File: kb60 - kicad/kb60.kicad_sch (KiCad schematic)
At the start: 0 parts

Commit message: made schematic for led matrix
also imported scottokeebs library
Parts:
- added D1, D10, D11, D12, D13, D14, D15, D16, D17, D18, D19, D2, D20, D21, D22, D23, D24, D25, D26, D27, D28, D29, D3, D30, D31, D32, D33, D34, D35, D36, D37, D38, D39, D4, D40, D41, D43, D44, D45, D46, D47, D48, D49, D5, D50, D51, D52, D53, D54, D55, D56, D57, D58, D59, D6, D60, D61, D62, D63, D67, D7, D71, D72, D73, D74, D75, D8, D9: Diode, symbol scottokeebs:Placeholder_Diode
- added S1, S10, S11, S12, S13, S14, S15, S16, S17, S18, S19, S2, S20, S21, S22, S23, S24, S25, S26, S27, S28, S29, S3, S30, S31, S32, S33, S34, S35, S36, S37, S38, S39, S4, S40, S41, S43, S44, S45, S46, S47, S48, S49, S5, S50, S51, S52, S53, S54, S55, S56, S57, S58, S59, S6, S60, S61, S62, S63, S67, S7, S71, S72, S73, S74, S75, S8, S9: Keyswitch, symbol scottokeebs:Placeholder_Keyswitch
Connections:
- new net: D16.1 (K), D17.1 (K), D18.1 (K), D19.1 (K), D20.1 (K), D21.1 (K), D22.1 (K), D23.1 (K), D24.1 (K), D25.1 (K), D26.1 (K), D27.1 (K), D28.1 (K), D29.1 (K), D30.1 (K)
- new net: D22.2 (A), S22.2
- new net: D46.1 (K), D47.1 (K), D48.1 (K), D49.1 (K), D50.1 (K), D51.1 (K), D52.1 (K), D53.1 (K), D54.1 (K), D55.1 (K), D56.1 (K), D57.1 (K), D58.1 (K), D59.1 (K), D60.1 (K)
- new net: D59.2 (A), S59.2
- new net: S1.1, S16.1, S31.1, S46.1, S61.1
- new net: D16.2 (A), S16.2
- new net: S15.1, S30.1, S45.1, S60.1, S75.1
- new net: D15.2 (A), S15.2
- new net: D27.2 (A), S27.2
- new net: S11.1, S26.1, S41.1, S56.1, S71.1
- new net: D26.2 (A), S26.2
- new net: D1.1 (K), D10.1 (K), D11.1 (K), D12.1 (K), D13.1 (K), D14.1 (K), D15.1 (K), D2.1 (K), D3.1 (K), D4.1 (K), D5.1 (K), D6.1 (K), D7.1 (K), D8.1 (K), D9.1 (K)
- new net: D10.2 (A), S10.2
- new net: D13.2 (A), S13.2
- new net: D61.1 (K), D62.1 (K), D63.1 (K), D67.1 (K), D71.1 (K), D72.1 (K), D73.1 (K), D74.1 (K), D75.1 (K)
- new net: D74.2 (A), S74.2
- new net: S23.1, S38.1, S53.1, S8.1
- new net: D53.2 (A), S53.2
- new net: D75.2 (A), S75.2
- new net: S21.1, S36.1, S51.1, S6.1
- new net: D21.2 (A), S21.2
- new net: D11.2 (A), S11.2
- new net: D14.2 (A), S14.2
- new net: D71.2 (A), S71.2
- new net: D6.2 (A), S6.2
- new net: D67.2 (A), S67.2
- new net: D1.2 (A), S1.2
- new net: D48.2 (A), S48.2
- new net: S14.1, S29.1, S44.1, S59.1, S74.1
- new net: D29.2 (A), S29.2
- new net: D31.1 (K), D32.1 (K), D33.1 (K), D34.1 (K), D35.1 (K), D36.1 (K), D37.1 (K), D38.1 (K), D39.1 (K), D40.1 (K), D41.1 (K), D43.1 (K), D44.1 (K), D45.1 (K)
- new net: D39.2 (A), S39.2
- new net: D23.2 (A), S23.2
- new net: D44.2 (A), S44.2
- new net: D49.2 (A), S49.2
- new net: D60.2 (A), S60.2
- new net: D40.2 (A), S40.2
- new net: S12.1, S27.1, S57.1, S72.1
- new net: D57.2 (A), S57.2
- new net: S20.1, S35.1, S5.1, S50.1
- new net: D35.2 (A), S35.2
- new net: D50.2 (A), S50.2
- new net: D3.2 (A), S3.2
- new net: D19.2 (A), S19.2
- new net: S10.1, S25.1, S40.1, S55.1
- new net: D72.2 (A), S72.2
- new net: S24.1, S39.1, S54.1, S9.1
- new net: D9.2 (A), S9.2
- new net: S19.1, S34.1, S4.1, S49.1
- new net: D4.2 (A), S4.2
- new net: D17.2 (A), S17.2
- new net: S18.1, S3.1, S33.1, S48.1, S63.1
- new net: D33.2 (A), S33.2
- new net: D54.2 (A), S54.2
- new net: S22.1, S37.1, S52.1, S67.1, S7.1
- new net: D7.2 (A), S7.2
- new net: D63.2 (A), S63.2
- new net: D46.2 (A), S46.2
- new net: S17.1, S2.1, S32.1, S47.1, S62.1
- new net: D47.2 (A), S47.2
- new net: D34.2 (A), S34.2
- new net: D31.2 (A), S31.2
- new net: D38.2 (A), S38.2
- new net: D62.2 (A), S62.2
- new net: D24.2 (A), S24.2
- new net: D18.2 (A), S18.2
- new net: D32.2 (A), S32.2
- new net: D12.2 (A), S12.2
- new net: D20.2 (A), S20.2
- new net: D73.2 (A), S73.2
- new net: D5.2 (A), S5.2
- new net: D2.2 (A), S2.2
- new net: D36.2 (A), S36.2
- new net: D51.2 (A), S51.2
- new net: D41.2 (A), S41.2
- new net: D37.2 (A), S37.2
- new net: D25.2 (A), S25.2
- new net: D28.2 (A), S28.2
- new net: D55.2 (A), S55.2
- new net: S13.1, S28.1, S43.1, S58.1, S73.1
- new net: D52.2 (A), S52.2
- new net: D43.2 (A), S43.2
- new net: D56.2 (A), S56.2
- new net: D30.2 (A), S30.2
- new net: D61.2 (A), S61.2
- new net: D58.2 (A), S58.2
- new net: D45.2 (A), S45.2
- new net: D8.2 (A), S8.2

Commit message: completed schematic
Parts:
- added U1: Raspberry_Pi_Pico, ScottoKeebs_MCU:Raspberry_Pi_Pico, symbol scottokeebs:MCU_Raspberry_Pi_Pico
- D1, D10, D11, D12, D13, D14, D15, D16, D17, D18, D19, D2, D20, D21, D22, D23, D24, D25, D26, D27, D28, D29, D3, D30, D31, D32, D33, D34, D35, D36, D37, D38, D39, D4, D40, D41, D43, D44, D45, D46, D47, D48, D49, D5, D50, D51, D52, D53, D54, D55, D56, D57, D58, D59, D6, D60, D61, D62, D63, D67, D7, D71, D72, D73, D74, D75, D8, D9: footprint (none) -> ScottoKeebs_Components:Diode_DO-35
- S1, S10, S11, S12, S13, S14, S15, S16, S17, S18, S19, S2, S20, S21, S22, S23, S24, S25, S26, S27, S28, S29, S3, S30, S31, S32, S33, S34, S35, S36, S37, S38, S39, S4, S40, S41, S43, S44, S45, S46, S47, S48, S49, S5, S50, S51, S52, S53, S54, S55, S56, S57, S58, S59, S6, S60, S61, S62, S63, S67, S7, S71, S72, S73, S74, S75, S8, S9: footprint (none) -> ScottoKeebs_MX:MX_PCB_1.00u
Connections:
- net Row 1: now reaches D16.1 (K), D17.1 (K), D18.1 (K), D19.1 (K), D20.1 (K), D21.1 (K), D22.1 (K), D23.1 (K), D24.1 (K), D25.1 (K), D26.1 (K), D27.1 (K), D28.1 (K), D29.1 (K), D30.1 (K)
- net Row 1: now also U1.21 (GPIO16)
- net Row 3: now reaches D46.1 (K), D47.1 (K), D48.1 (K), D49.1 (K), D50.1 (K), D51.1 (K), D52.1 (K), D53.1 (K), D54.1 (K), D55.1 (K), D56.1 (K), D57.1 (K), D58.1 (K), D59.1 (K), D60.1 (K)
- net Row 3: now also U1.24 (GPIO18)
- net Column 0: now reaches S1.1, S16.1, S31.1, S46.1, S61.1
- net Column 0: now also U1.1 (GPIO0)
- net Column 14: now reaches S15.1, S30.1, S45.1, S60.1, S75.1
- net Column 14: now also U1.19 (GPIO14)
- net Column 10: now reaches S11.1, S26.1, S41.1, S56.1, S71.1
- net Column 10: now also U1.14 (GPIO10)
- net Row 0: now reaches D1.1 (K), D10.1 (K), D11.1 (K), D12.1 (K), D13.1 (K), D14.1 (K), D15.1 (K), D2.1 (K), D3.1 (K), D4.1 (K), D5.1 (K), D6.1 (K), D7.1 (K), D8.1 (K), D9.1 (K)
- net Row 0: now also U1.20 (GPIO15)
- net Row 4: now reaches D61.1 (K), D62.1 (K), D63.1 (K), D67.1 (K), D71.1 (K), D72.1 (K), D73.1 (K), D74.1 (K), D75.1 (K)
- net Row 4: now also U1.25 (GPIO19)
- net Column 7: now reaches S23.1, S38.1, S53.1, S8.1
- net Column 7: now also U1.10 (GPIO7)
- net Column 5: now reaches S21.1, S36.1, S51.1, S6.1
- net Column 5: now also U1.7 (GPIO5)
- net Column 13: now reaches S14.1, S29.1, S44.1, S59.1, S74.1
- net Column 13: now also U1.17 (GPIO13)
- net Row 2: now reaches D31.1 (K), D32.1 (K), D33.1 (K), D34.1 (K), D35.1 (K), D36.1 (K), D37.1 (K), D38.1 (K), D39.1 (K), D40.1 (K), D41.1 (K), D43.1 (K), D44.1 (K), D45.1 (K)
- net Row 2: now also U1.22 (GPIO17)
- net Column 11: now reaches S12.1, S27.1, S57.1, S72.1
- net Column 11: now also U1.15 (GPIO11)
- net Column 4: now reaches S20.1, S35.1, S5.1, S50.1
- net Column 4: now also U1.6 (GPIO4)
- net Column 9: now reaches S10.1, S25.1, S40.1, S55.1
- net Column 9: now also U1.12 (GPIO9)
- net Column 8: now reaches S24.1, S39.1, S54.1, S9.1
- net Column 8: now also U1.11 (GPIO8)
- net Column 3: now reaches S19.1, S34.1, S4.1, S49.1
- net Column 3: now also U1.5 (GPIO3)
- net Column 2: now reaches S18.1, S3.1, S33.1, S48.1, S63.1
- net Column 2: now also U1.4 (GPIO2)
- net Column 6: now reaches S22.1, S37.1, S52.1, S67.1, S7.1
- net Column 6: now also U1.9 (GPIO6)
- net Column 1: now reaches S17.1, S2.1, S32.1, S47.1, S62.1
- net Column 1: now also U1.2 (GPIO1)
- net Column 12: now reaches S13.1, S28.1, S43.1, S58.1, S73.1
- net Column 12: now also U1.16 (GPIO12)
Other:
- moved on the sheet: D1, D10, D11, D12, D13, D14, D15, D16, D17, D18, D19, D2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

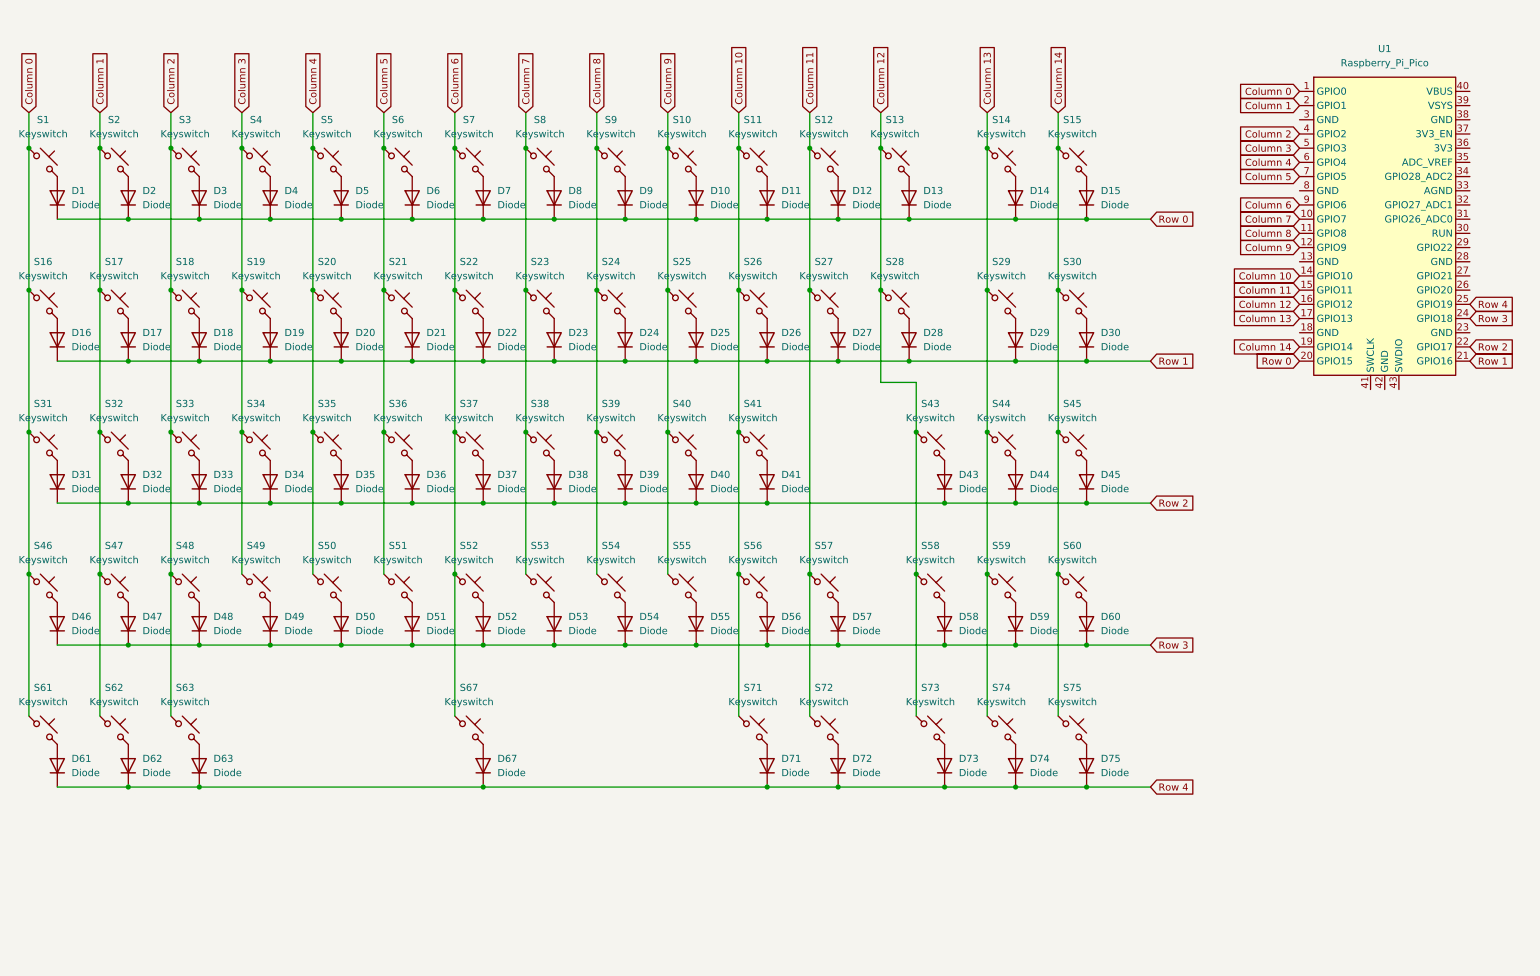
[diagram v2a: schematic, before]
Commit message: started pcb design
placed keys in rough places
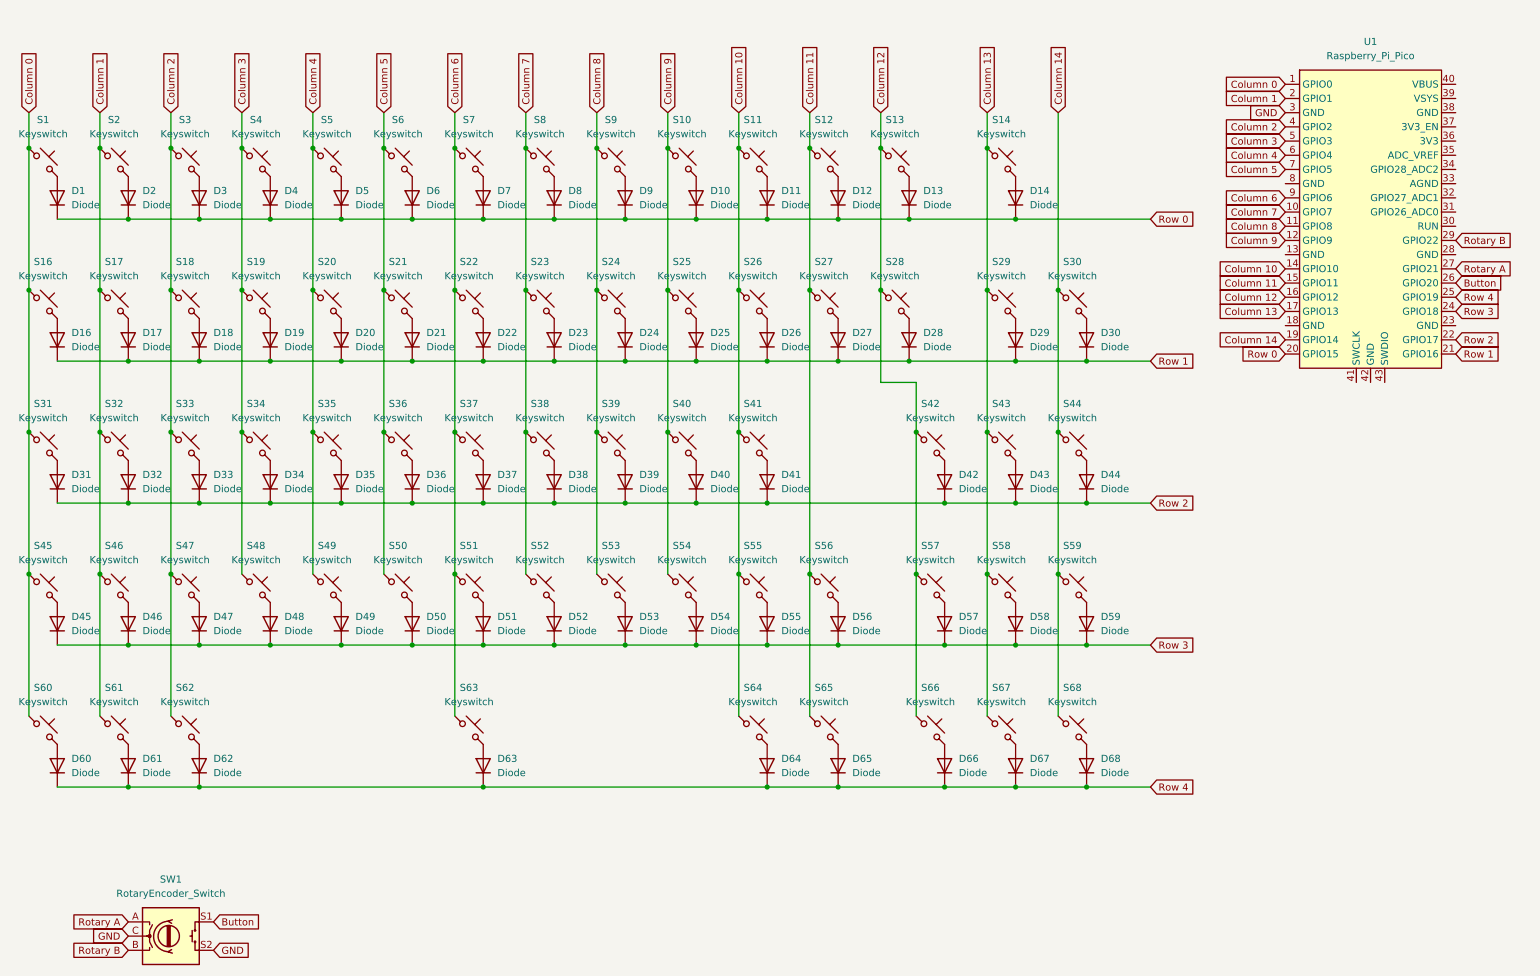
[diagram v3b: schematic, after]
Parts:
- removed D15: Diode, ScottoKeebs_Components:Diode_DO-35, symbol scottokeebs:Placeholder_Diode
- removed S15: Keyswitch, ScottoKeebs_MX:MX_PCB_1.00u, symbol scottokeebs:Placeholder_Keyswitch
- added SW1: RotaryEncoder_Switch, Rotary_Encoder:RotaryEncoder_Alps_EC12E-Switch_Vertical_H20mm, symbol Device:RotaryEncoder_Switch
- renumbered D43 to D42, D44 to D43, D45 to D44, D46 to D45, D47 to D46, D48 to D47, D49 to D48, D50 to D49, D51 to D50, D52 to D51, D53 to D52, D54 to D53, D55 to D54, D56 to D55, D57 to D56, D58 to D57, D59 to D58, D60 to D59, D61 to D60, D62 to D61, D63 to D62, D67 to D63, D71 to D64, D72 to D65, D73 to D66, D74 to D67, D75 to D68, S43 to S42, S44 to S43, S45 to S44, S46 to S45, S47 to S46, S48 to S47, S49 to S48, S50 to S49, S51 to S50, S52 to S51, S53 to S52, S54 to S53, S55 to S54, S56 to S55, S57 to S56, S58 to S57, S59 to S58, S60 to S59, S61 to S60, S62 to S61, S63 to S62, S67 to S63, S71 to S64, S72 to S65, S73 to S66, S74 to S67, S75 to S68
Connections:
- net Button: now reaches U1.26 (GPIO20)
- net Button: now also SW1.S1
- net Rotary A: now reaches U1.27 (GPIO21)
- net Rotary A: now also SW1.A
- net Rotary B: now reaches U1.29 (GPIO22)
- net Rotary B: now also SW1.B
- net GND: now reaches U1.3 (GND)
- net GND: now also SW1.C, SW1.S2
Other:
- moved on the sheet: U1

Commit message: added rotary encoder to switch matrix
as it has a switch as well
also added my keyboard layout that i wanted as a guideline for pcb placement
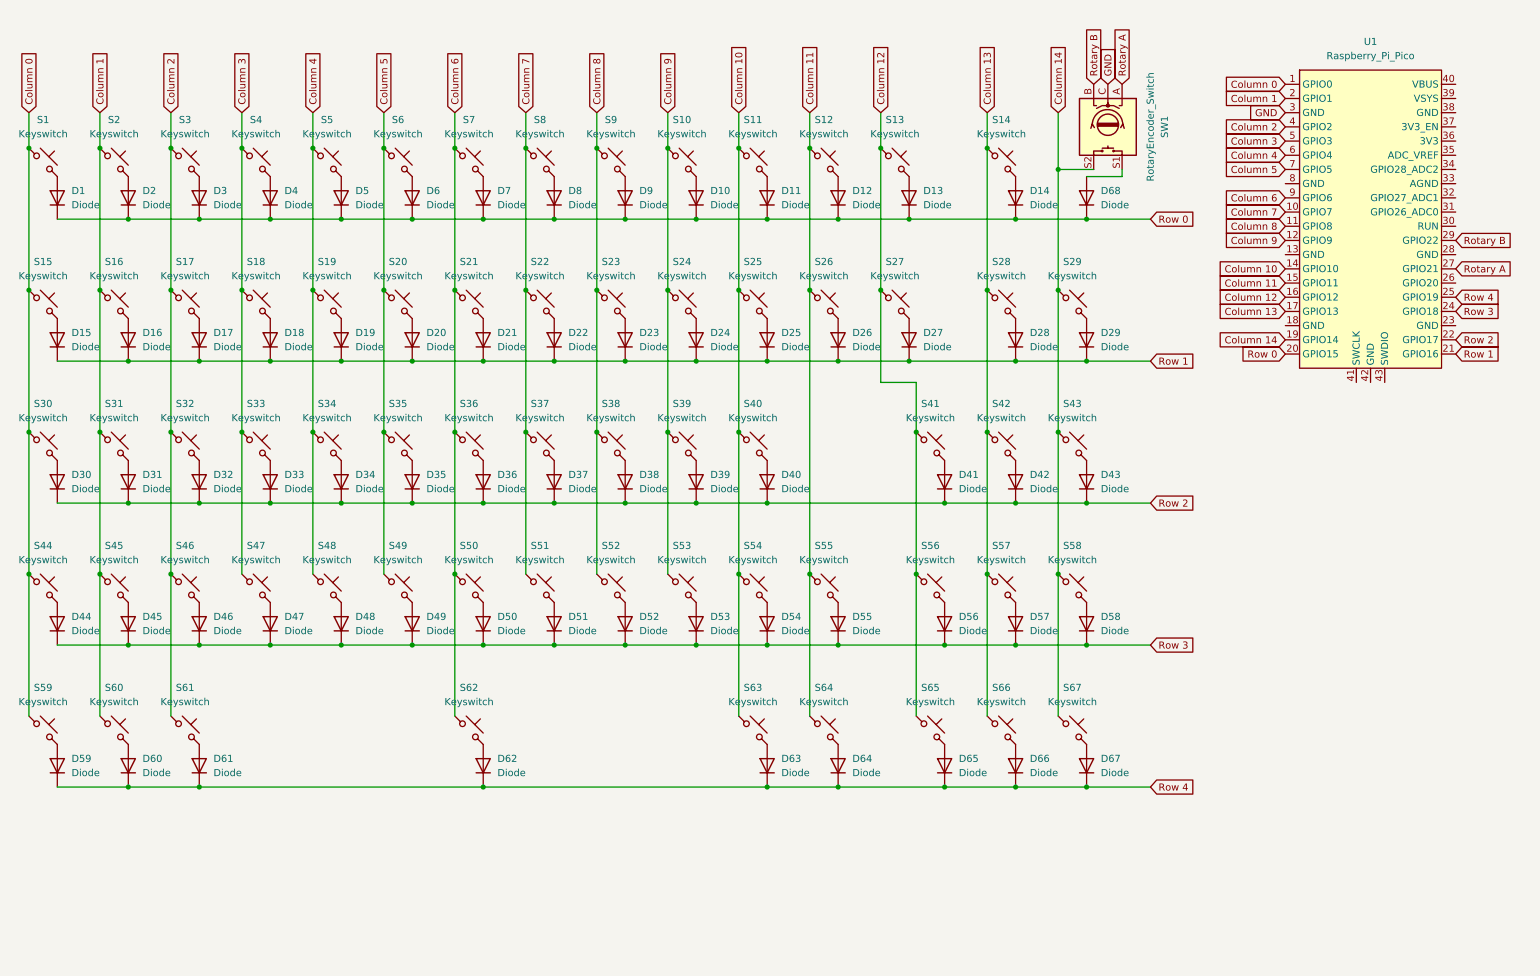
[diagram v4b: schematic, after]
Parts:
- added D68: Diode, ScottoKeebs_Components:Diode_DO-35, symbol scottokeebs:Placeholder_Diode
- renumbered D16 to D15, D17 to D16, D18 to D17, D19 to D18, D20 to D19, D21 to D20, D22 to D21, D23 to D22, D24 to D23, D25 to D24, D26 to D25, D27 to D26, D28 to D27, D29 to D28, D30 to D29, D31 to D30, D32 to D31, D33 to D32, D34 to D33, D35 to D34, D36 to D35, D37 to D36, D38 to D37, D39 to D38, D40 to D39, D41 to D40, D42 to D41, D43 to D42, D44 to D43, D45 to D44, D46 to D45, D47 to D46, D48 to D47, D49 to D48, D50 to D49, D51 to D50, D52 to D51, D53 to D52, D54 to D53, D55 to D54, D56 to D55, D57 to D56, D58 to D57, D59 to D58, D60 to D59, D61 to D60, D62 to D61, D63 to D62, D64 to D63, D65 to D64, D66 to D65, D67 to D66, D68 to D67, S16 to S15, S17 to S16, S18 to S17, S19 to S18, S20 to S19, S21 to S20, S22 to S21, S23 to S22, S24 to S23, S25 to S24, S26 to S25, S27 to S26, S28 to S27, S29 to S28, S30 to S29, S31 to S30, S32 to S31, S33 to S32, S34 to S33, S35 to S34, S36 to S35, S37 to S36, S38 to S37, S39 to S38, S40 to S39, S41 to S40, S42 to S41, S43 to S42, S44 to S43, S45 to S44, S46 to S45, S47 to S46, S48 to S47, S49 to S48, S50 to S49, S51 to S50, S52 to S51, S53 to S52, S54 to S53, S55 to S54, S56 to S55, S57 to S56, S58 to S57, S59 to S58, S60 to S59, S61 to S60, S62 to S61, S63 to S62, S64 to S63, S65 to S64, S66 to S65, S67 to S66, S68 to S67
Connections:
- net Column 14: now also SW1.S2
- net GND: no longer SW1.S2
- net Row 0: now also D68.1 (K)
- net Button: no longer names the net of SW1.S1
- net Button: now also D68.2 (A); no longer U1.26 (GPIO20)
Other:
- moved on the sheet: SW1
